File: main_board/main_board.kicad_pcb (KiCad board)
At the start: 4 copper layers, 50 x 50 mm, 76 parts, among them J1 USB Port, J2 I2C, J3 LED, J4 Left_Mic, J5 Left_Speaker, J6 Right_Mic, J7 Right_Speaker, J8 I2C, Q1 MMBT3904, Q2 MMBT3904, SW1 SW_Push, SW2 SW_Push, SW3 SW_Push, U1 AMS1117-3.3, U2 CH340K, U4 Headphone Jack, U5 WM8988LGECN/V, U6 WM8988LGECN/V, U7 AMS1117-3.3, U8 ESP32-WROOM-32E

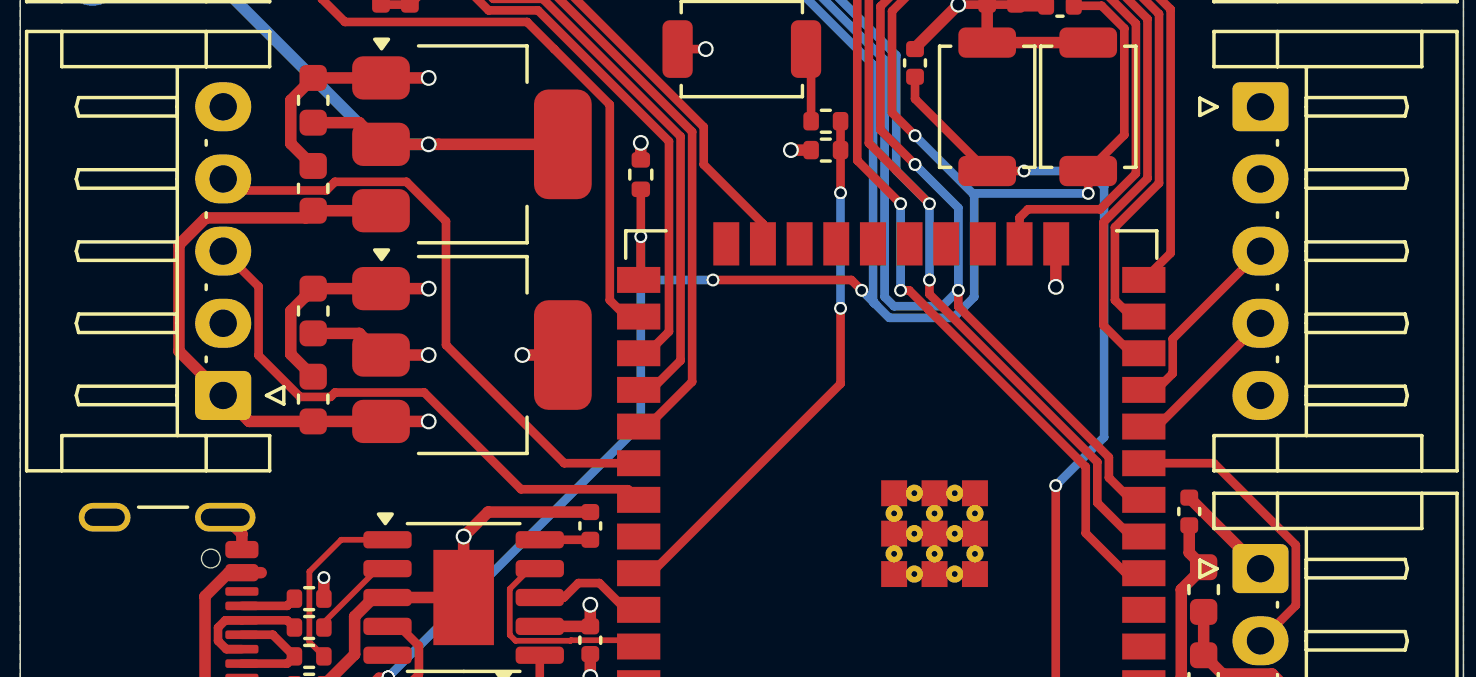
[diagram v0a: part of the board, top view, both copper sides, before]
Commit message: fix: missing I2C pullup resistors
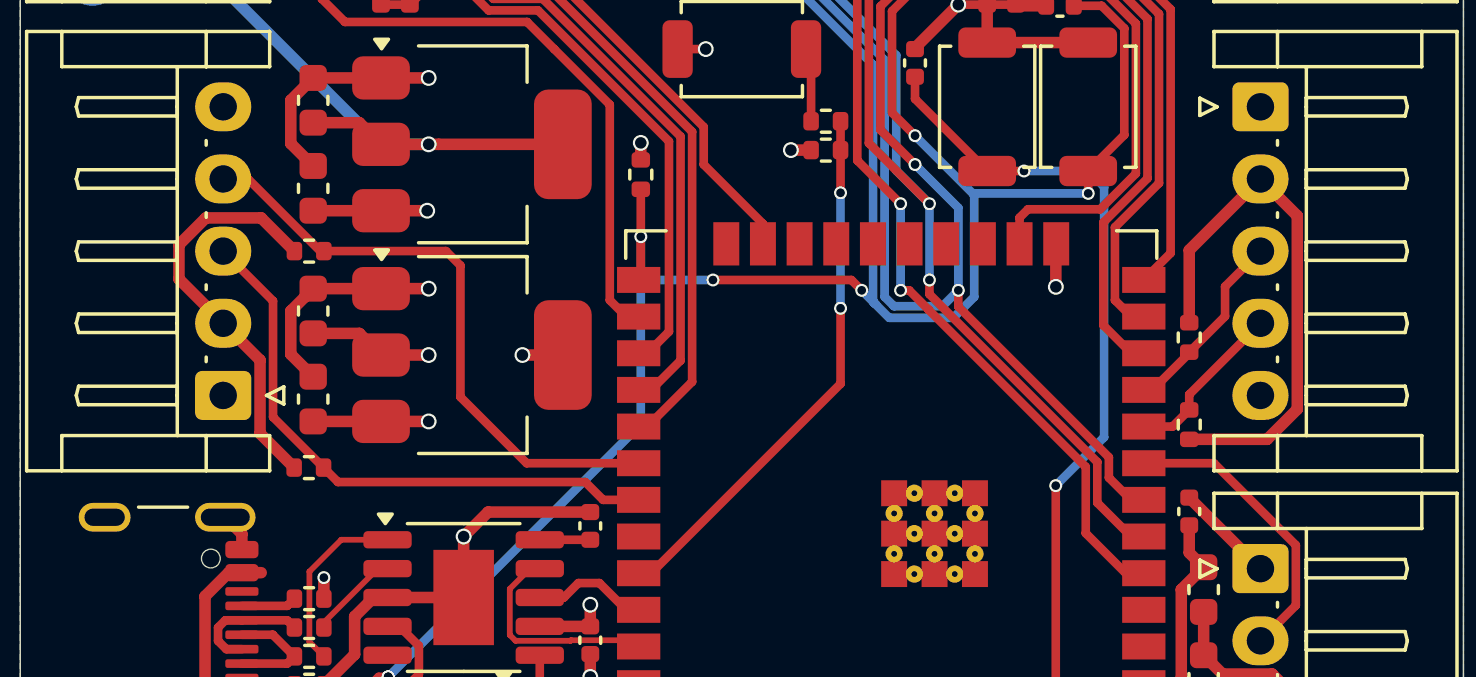
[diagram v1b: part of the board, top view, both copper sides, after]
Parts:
- added R12: 5.1k, Resistor_SMD:R_0402_1005Metric, F.Cu at (163.5, 107.0)
- added R15: 5.1k, Resistor_SMD:R_0402_1005Metric, F.Cu at (163.5, 104.0)
- added R16: 5.1k, Resistor_SMD:R_0402_1005Metric, F.Cu at (133.0, 101.0)
- added R17: 5.1k, Resistor_SMD:R_0402_1005Metric, F.Cu at (133.0, 108.5)
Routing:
- net +3V3D: track 38.3 -> 71.2 mm
- net +5V: track 31.7 -> 18.8 mm, vias 2 -> 3
- net /Out_DAT1: track 19.5 -> 20.3 mm

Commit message: finish v1.0
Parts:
- removed C7, C8: 100n, Capacitor_SMD:C_0402_1005Metric
- added R18: 1k, Resistor_SMD:R_0402_1005Metric, F.Cu at (154.0, 93.0)
- added R19: 1k, Resistor_SMD:R_0402_1005Metric, F.Cu at (154.0, 95.0)
- turned SW1 to 90 degrees
- turned SW2 to 90 degrees
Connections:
- SW1 pad 2: /GPIO0 -> Net-(R18-Pad1)
- SW2 pad 2: /MCU_EN -> Net-(R19-Pad1)
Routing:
- net Net-(R19-Pad1): track 0.00 -> 13.9 mm
- net /GPIO0: track 94.7 -> 83.2 mm, vias 8 -> 6
- net Net-(R18-Pad1): track 0.00 -> 6.75 mm
- net GND: track 90.8 -> 86.4 mm, vias 13 -> 14
- net /MCU_EN: track 54.0 -> 50.0 mm
